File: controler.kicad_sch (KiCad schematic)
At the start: 38 parts, among them J1 USB_BOOT, J12 Conn_01x04_Pin, J2 Conn_ARM_JTAG_SWD_10, SW1 SW_DIP_x08, U1 RP2040, U2 W25Q128JVS, U3 NCP1117-3.3_SOT223, Y1 12MHz

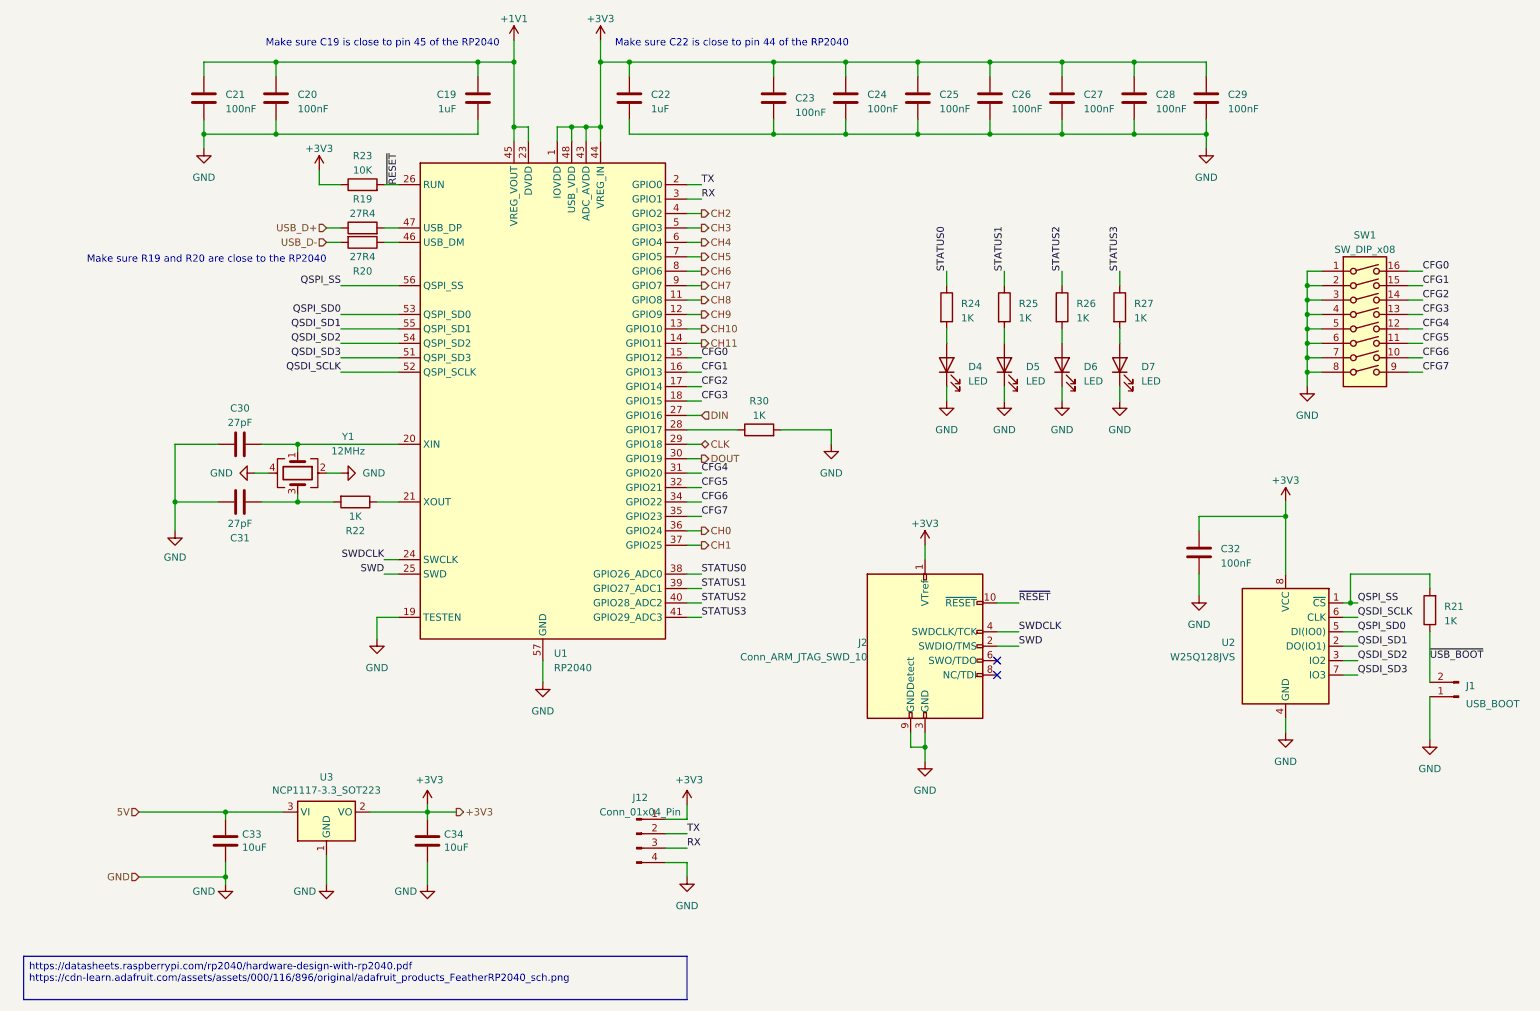
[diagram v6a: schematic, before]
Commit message: Added optional pull up resistor for flash chip
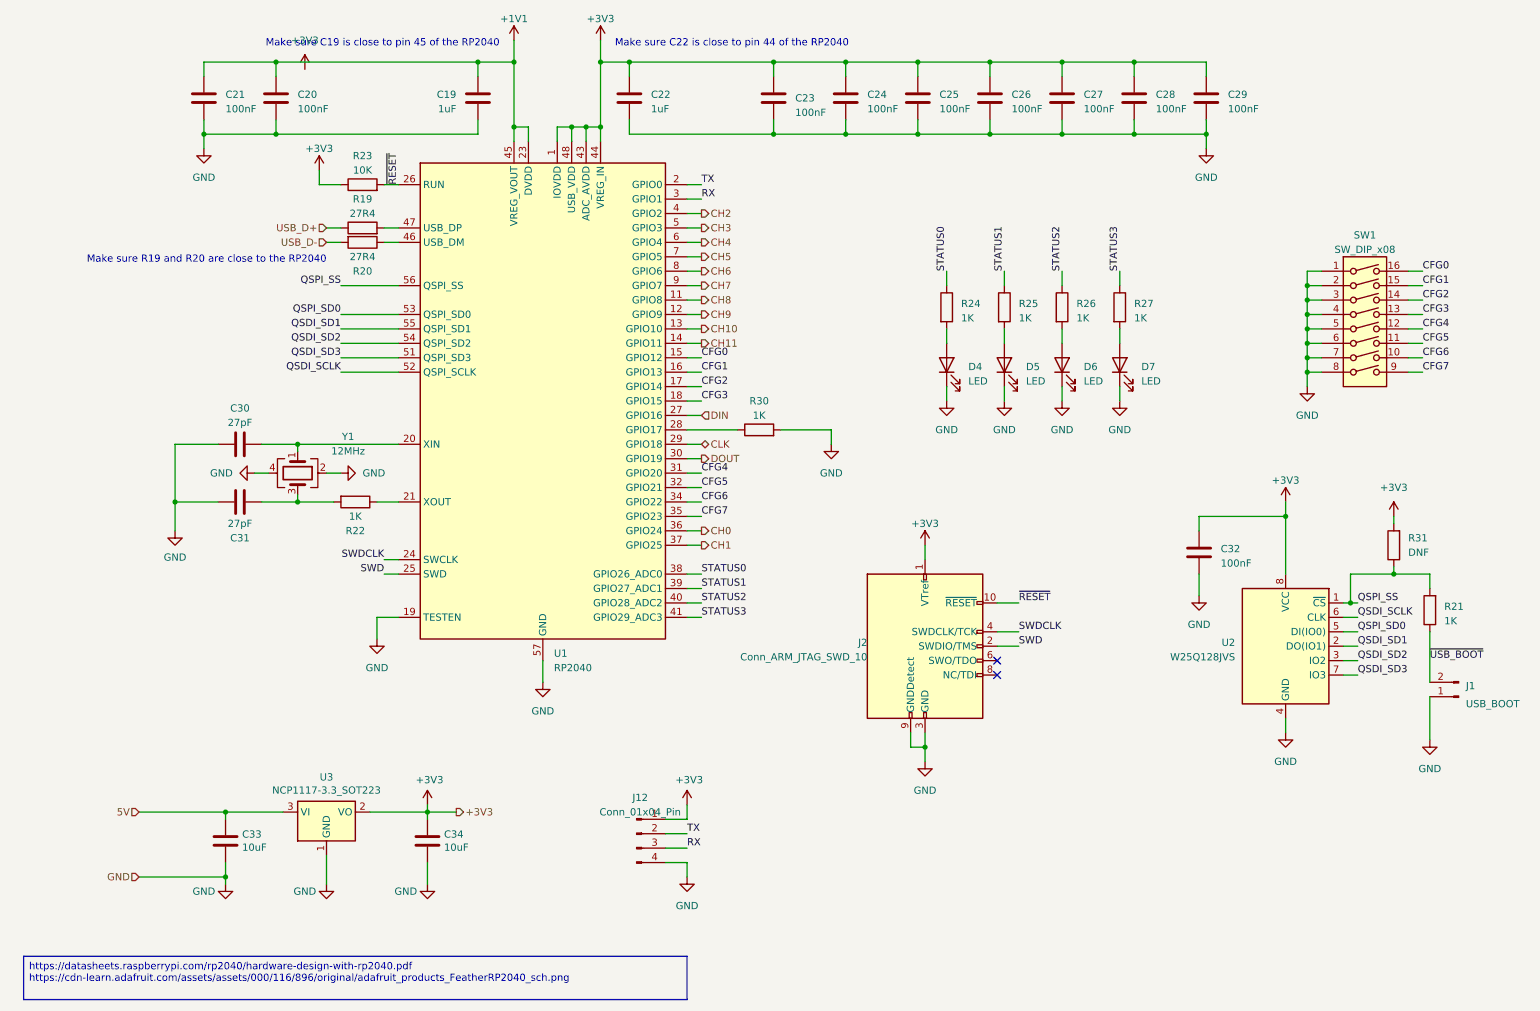
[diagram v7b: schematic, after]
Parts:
- added R31: DNF, Resistor_SMD:R_0603_1608Metric, symbol Device:R
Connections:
- net +3V3: now also R31.2
- net QSPI_SS: now also R31.1
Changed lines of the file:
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@@
 	)
 	(junction
+		(at 255.27 120.65)
+		(diameter 0)
+		(color 0 0 0 0)
+	)
+	(junction
 		(at 196.85 30.48)
 		(diameter 0)
@@
 	(wire
 		(pts
+			(xy 255.27 110.49) (xy 255.27 111.76)
+		)
+		(stroke
+			(width 0)
+			(type default)
+		)
+	)
+	(wire
+		(pts
 			(xy 69.85 85.09) (xy 80.01 85.09)
 		)
@@
 	(wire
 		(pts
+			(xy 255.27 120.65) (xy 247.65 120.65)
+		)
+		(stroke
+			(width 0)
+			(type default)
+		)
+	)
+	(wire
+		(pts
 			(xy 240.03 72.39) (xy 242.57 72.39)
 		)
@@
 	(wire
 		(pts
+			(xy 255.27 119.38) (xy 255.27 120.65)
+		)
+		(stroke
+			(width 0)
+			(type default)
+		)
+	)
+	(wire
+		(pts
 			(xy 130.81 171.45) (xy 130.81 173.99)
 		)
@@
 	(wire
 		(pts
-			(xy 261.62 120.65) (xy 247.65 120.65)
+			(xy 261.62 120.65) (xy 255.27 120.65)
 		)
 		(stroke
@@
 	)
 	(symbol
+		(lib_name "+3V3_1")
+		(lib_id "power:+3V3")
+		(at 63.5 31.75 0)
+		(unit 1)
+		(exclude_from_sim no)
+		(in_bom yes)
+		(on_board yes)
+		(dnp no)
+		(fields_autoplaced yes)
+		(property "Reference" "#PWR059"
+			(at 63.5 35.56 0)
+			(effects
+				(font
+					(size 1.27 1.27)
+				)
+				(hide yes)
+			)
+		)
+		(property "Value" "+3V3"
+			(at 63.5 26.67 0)
+			(effects
+				(font
+					(size 1.27 1.27)
+				)
+			)
+		)
+		(property "Footprint" ""
+			(at 63.5 31.75 0)
+			(effects
+				(font
+					(size 1.27 1.27)
+				)
+				(hide yes)
+			)
+		)
+		(property "Datasheet" ""
+			(at 63.5 31.75 0)
+			(effects
+				(font
+					(size 1.27 1.27)
+				)
+				(hide yes)
+			)
+		)
+		(property "Description" "Power symbol creates a global label with name \"+3V3\""
+			(at 63.5 31.75 0)
+			(effects
+				(font
+					(size 1.27 1.27)
+				)
+				(hide yes)
+			)
+		)
+		(pin "1"
+		)
+		(instances
+			(project ""
+				(path "/c494d399-9c3e-4fb0-8fd0-96c74769e433/c3e5f29d-a8aa-4f99-a65b-6663a6477720"
+					(reference "#PWR059")
+					(unit 1)
+				)
+			)
+		)
+	)
+	(symbol
 		(lib_id "Device:R")
 		(at 73.66 62.23 270)
@@
 	)
 	(symbol
+		(lib_id "Device:R")
+		(at 255.27 115.57 180)
+		(unit 1)
+		(exclude_from_sim no)
+		(in_bom yes)
+		(on_board yes)
+		(dnp no)
+		(fields_autoplaced yes)
+		(property "Reference" "R31"
+			(at 257.81 114.2999 0)
+			(effects
+				(font
+					(size 1.27 1.27)
+				)
+				(justify right)
+			)
+		)
+		(property "Value" "DNF"
+			(at 257.81 116.8399 0)
+			(effects
+				(font
+					(size 1.27 1.27)
+				)
+				(justify right)
+			)
+		)
+		(property "Footprint" "Resistor_SMD:R_0603_1608Metric"
+			(at 257.048 115.57 90)
+			(effects
+				(font
+					(size 1.27 1.27)
+				)
+				(hide yes)
+			)
+		)
+		(property "Datasheet" "~"
+			(at 255.27 115.57 0)
+			(effects
+				(font
+					(size 1.27 1.27)
+				)
+				(hide yes)
+			)
+		)
+		(property "Description" ""
+			(at 255.27 115.57 0)
+			(effects
+				(font
+					(size 1.27 1.27)
+				)
+				(hide yes)
+			)
+		)
+		(pin "1"
+		)
+		(pin "2"
+		)
+		(instances
+			(project "SmartishFairy"
+				(path "/c494d399-9c3e-4fb0-8fd0-96c74769e433/c3e5f29d-a8aa-4f99-a65b-6663a6477720"
+					(reference "R31")
+					(unit 1)
+				)
+			)
+		)
+	)
+	(symbol
 		(lib_id "Device:C")
 		(at 45.72 36.83 0)
@@
 					(unit 1)
 				)
+			)
+		)
+	)
+	(symbol
+		(lib_name "+3V3_2")
+		(lib_id "power:+3V3")
+		(at 255.27 110.49 0)
+		(unit 1)
+		(exclude_from_sim no)
+		(in_bom yes)
+		(on_board yes)
+		(dnp no)
+		(fields_autoplaced yes)
+		(property "Reference" "#PWR060"
+			(at 255.27 114.3 0)
+			(effects
+				(font
+					(size 1.27 1.27)
+				)
+				(hide yes)
+			)
+		)
+		(property "Value" "+3V3"
+			(at 255.27 105.41 0)
+			(effects
+				(font
+					(size 1.27 1.27)
+				)
+			)
+		)
+		(property "Footprint" ""
+			(at 255.27 110.49 0)
+			(effects
+				(font
+					(size 1.27 1.27)
+				)
+				(hide yes)
+			)
+		)
+		(property "Datasheet" ""
+			(at 255.27 110.49 0)
+			(effects
+				(font
+					(size 1.27 1.27)
+				)
+				(hide yes)
+			)
+		)
+		(property "Description" "Power symbol creates a global label with name \"+3V3\""
+			(at 255.27 110.49 0)
+			(effects
+				(font
+					(size 1.27 1.27)
+				)
+				(hide yes)
+			)
+		)
+		(pin "1"
+		)
+		(instances
+			(project ""
+				(path "/c494d399-9c3e-4fb0-8fd0-96c74769e433/c3e5f29d-a8aa-4f99-a65b-6663a6477720"
+					(reference "#PWR060")
+					(unit 1)
+				)

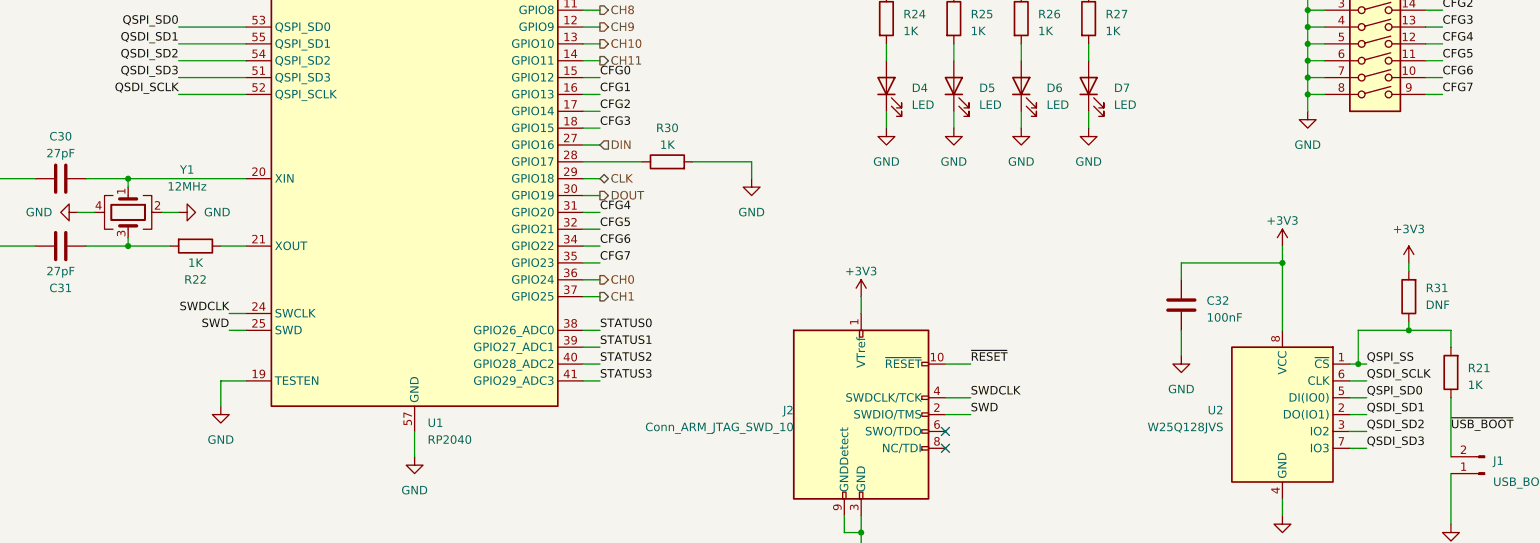
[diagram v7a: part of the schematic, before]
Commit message: Added a few JLC part number
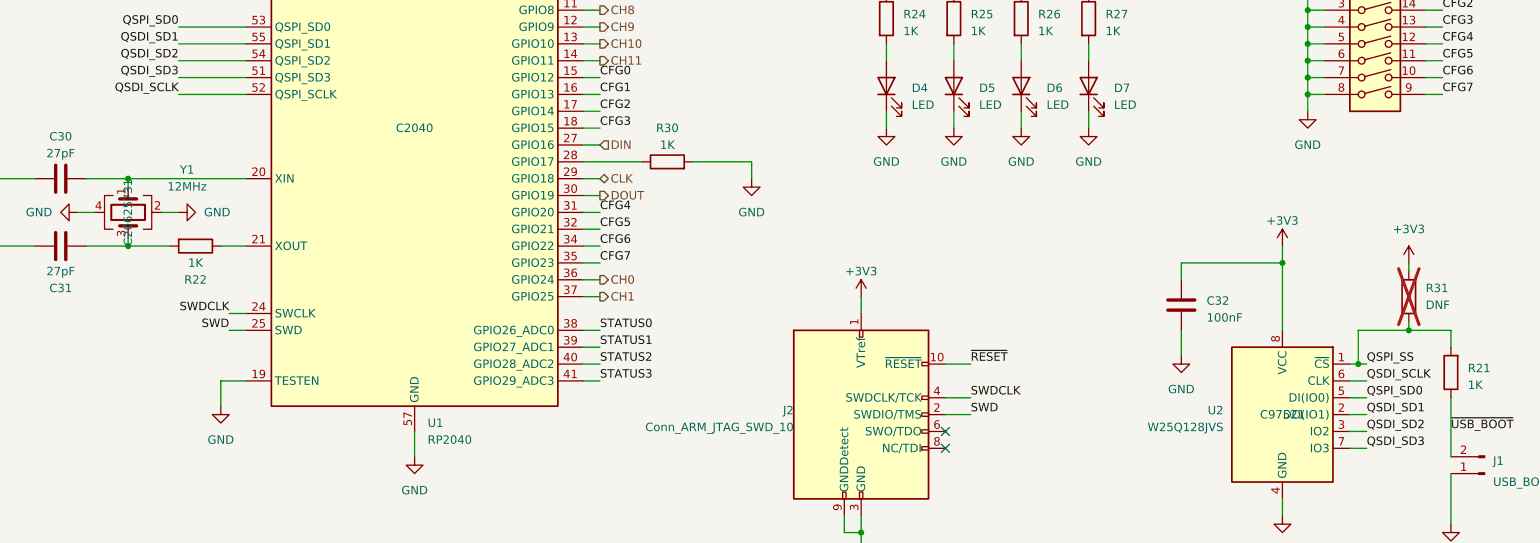
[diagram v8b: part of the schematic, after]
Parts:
- R31: now not fitted
- U1: LCSC (none) -> C2040
- U2: LCSC (none) -> C97521
- Y1: LCSC (none) -> C20625731
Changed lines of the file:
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@@
+			)
+		)
+		(property "LCSC" "C20625731"
+			(at 62.23 102.87 0)
+			(effects
+				(font
+					(size 1.27 1.27)
+				)
 			)
 		)
@@
 			)
 		)
+		(property "LCSC" "C97521"
+			(at 236.22 133.35 0)
+			(effects
+				(font
+					(size 1.27 1.27)
+				)
+			)
+		)
 		(pin "1"
 		)
@@
 			)
 		)
+		(property "LCSC" "C2040"
+			(at 105.41 90.17 0)
+			(effects
+				(font
+					(size 1.27 1.27)
+				)
+			)
+		)
 		(pin "1"
 		)
@@
 		(in_bom yes)
 		(on_board yes)
-		(dnp no)
+		(dnp yes)
 		(fields_autoplaced yes)
 		(property "Reference" "R31"
